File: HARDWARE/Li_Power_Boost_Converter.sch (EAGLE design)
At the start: 20 parts, among them U1 TPS61200

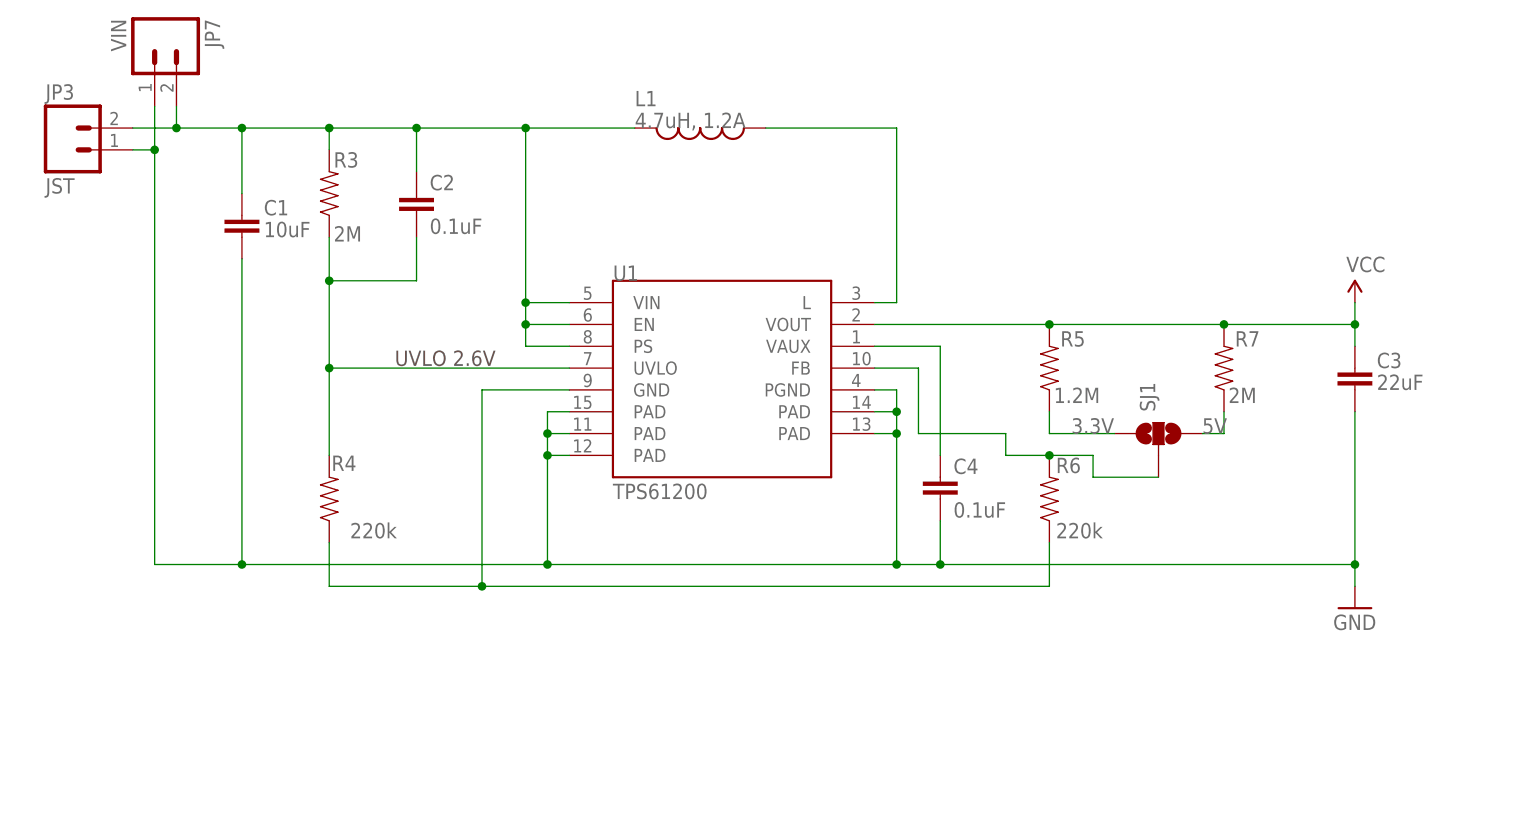
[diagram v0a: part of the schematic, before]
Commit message: Schematic Cleanup / Heat Sink
Cleaned up a few nets and removed on heat sink for better flow
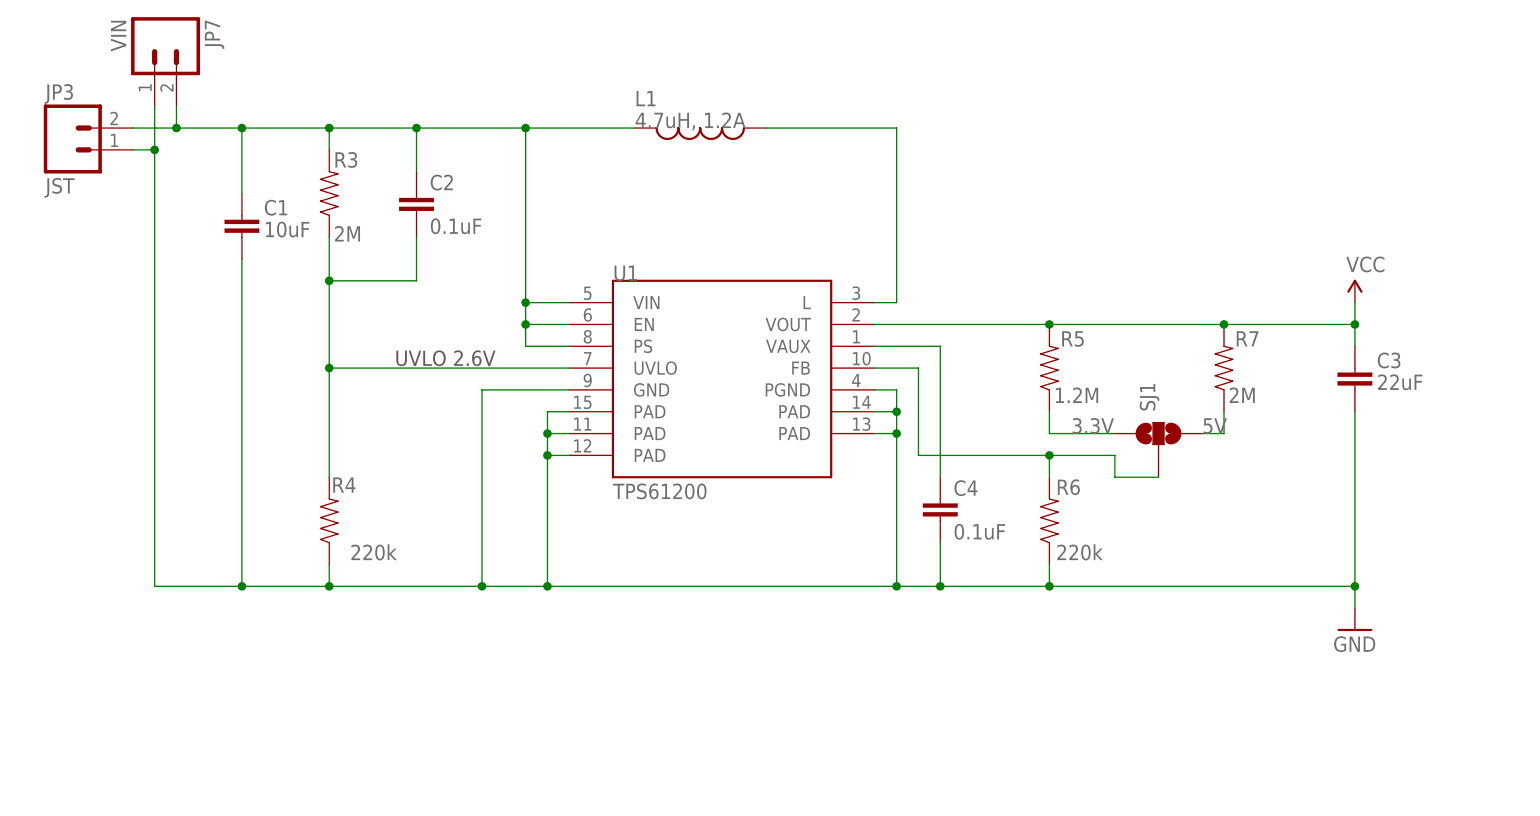
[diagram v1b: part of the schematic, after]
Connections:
- removed net GND1: R4.1, R6.1, U1.GND
- net GND: now also R4.1, R6.1, U1.GND
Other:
- moved on the sheet: C4, R4, R6
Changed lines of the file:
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@@
 <instance part="U1" gate="G$1" x="106.68" y="101.6"/>
 <instance part="C2" gate="G$1" x="71.12" y="119.38"/>
-<instance part="C4" gate="G$1" x="132.08" y="86.36"/>
+<instance part="C4" gate="G$1" x="132.08" y="83.82"/>
 <instance part="R3" gate="G$1" x="60.96" y="121.92" smashed="yes" rot="R90">
 <attribute name="NAME" x="61.468" y="124.9426" size="1.778" layer="95"/>
 <attribute name="VALUE" x="61.468" y="116.332" size="1.778" layer="96"/>
 </instance>
-<instance part="R4" gate="G$1" x="60.96" y="86.36" smashed="yes" rot="R90">
-<attribute name="NAME" x="61.214" y="89.6366" size="1.778" layer="95"/>
-<attribute name="VALUE" x="68.834" y="83.566" size="1.778" layer="96" rot="R180"/>
+<instance part="R4" gate="G$1" x="60.96" y="83.82" smashed="yes" rot="R90">
+<attribute name="NAME" x="61.214" y="87.0966" size="1.778" layer="95"/>
+<attribute name="VALUE" x="68.834" y="81.026" size="1.778" layer="96" rot="R180"/>
 </instance>
 <instance part="R5" gate="G$1" x="144.78" y="101.6" smashed="yes" rot="R90">
@@
 <attribute name="VALUE" x="145.288" y="97.536" size="1.778" layer="96"/>
 </instance>
-<instance part="R6" gate="G$1" x="144.78" y="86.36" smashed="yes" rot="R90">
-<attribute name="NAME" x="145.542" y="89.3826" size="1.778" layer="95"/>
-<attribute name="VALUE" x="145.542" y="81.788" size="1.778" layer="96"/>
-</instance>
-<instance part="GND1" gate="1" x="180.34" y="73.66"/>
+<instance part="R6" gate="G$1" x="144.78" y="83.82" smashed="yes" rot="R90">
+<attribute name="NAME" x="145.542" y="86.8426" size="1.778" layer="95"/>
+<attribute name="VALUE" x="145.542" y="79.248" size="1.778" layer="96"/>
+</instance>
+<instance part="GND1" gate="1" x="180.34" y="71.12"/>
 <instance part="GND2" gate="1" x="208.28" y="99.06"/>
 <instance part="R7" gate="G$1" x="165.1" y="101.6" smashed="yes" rot="R90">
@@
 <net name="N$1" class="0">
 <segment>
-<wire x1="132.08" y1="91.44" x2="132.08" y2="104.14" width="0.1524" layer="91"/>
+<wire x1="132.08" y1="88.9" x2="132.08" y2="104.14" width="0.1524" layer="91"/>
 <wire x1="132.08" y1="104.14" x2="124.46" y2="104.14" width="0.1524" layer="91"/>
 <pinref part="U1" gate="G$1" pin="VAUX"/>
@@
 <wire x1="60.96" y1="116.84" x2="60.96" y2="111.76" width="0.1524" layer="91"/>
 <wire x1="60.96" y1="111.76" x2="60.96" y2="101.6" width="0.1524" layer="91"/>
-<wire x1="60.96" y1="101.6" x2="60.96" y2="91.44" width="0.1524" layer="91"/>
+<wire x1="60.96" y1="101.6" x2="60.96" y2="88.9" width="0.1524" layer="91"/>
 <wire x1="88.9" y1="101.6" x2="60.96" y2="101.6" width="0.1524" layer="91"/>
 <wire x1="71.12" y1="116.84" x2="71.12" y2="111.76" width="0.1524" layer="91"/>
@@
 <net name="FB" class="0">
 <segment>
-<wire x1="129.54" y1="93.98" x2="139.7" y2="93.98" width="0.1524" layer="91"/>
-<wire x1="129.54" y1="93.98" x2="129.54" y2="101.6" width="0.1524" layer="91"/>
-<wire x1="129.54" y1="101.6" x2="124.46" y2="101.6" width="0.1524" layer="91"/>
-<wire x1="157.48" y1="88.9" x2="149.86" y2="88.9" width="0.1524" layer="91"/>
-<wire x1="149.86" y1="88.9" x2="149.86" y2="91.44" width="0.1524" layer="91"/>
-<wire x1="149.86" y1="91.44" x2="144.78" y2="91.44" width="0.1524" layer="91"/>
-<wire x1="144.78" y1="91.44" x2="139.7" y2="91.44" width="0.1524" layer="91"/>
-<wire x1="139.7" y1="91.44" x2="139.7" y2="93.98" width="0.1524" layer="91"/>
+<wire x1="144.78" y1="91.44" x2="152.4" y2="91.44" width="0.1524" layer="91"/>
+<wire x1="152.4" y1="91.44" x2="152.4" y2="88.9" width="0.1524" layer="91"/>
+<pinref part="SJ1" gate="G$1" pin="2"/>
+<wire x1="152.4" y1="88.9" x2="157.48" y2="88.9" width="0.1524" layer="91"/>
+<pinref part="R6" gate="G$1" pin="2"/>
+<wire x1="144.78" y1="88.9" x2="144.78" y2="91.44" width="0.1524" layer="91"/>
 <junction x="144.78" y="91.44"/>
+<wire x1="144.78" y1="91.44" x2="129.54" y2="91.44" width="0.1524" layer="91"/>
 <pinref part="U1" gate="G$1" pin="FB"/>
-<pinref part="R6" gate="G$1" pin="2"/>
-<pinref part="SJ1" gate="G$1" pin="2"/>
+<wire x1="124.46" y1="101.6" x2="129.54" y2="101.6" width="0.1524" layer="91"/>
+<wire x1="129.54" y1="101.6" x2="129.54" y2="91.44" width="0.1524" layer="91"/>
 </segment>
 </net>
@@
 <net name="GND" class="0">
 <segment>
-<wire x1="132.08" y1="83.82" x2="132.08" y2="78.74" width="0.1524" layer="91"/>
-<wire x1="50.8" y1="114.3" x2="50.8" y2="78.74" width="0.1524" layer="91"/>
-<wire x1="40.64" y1="127" x2="40.64" y2="78.74" width="0.1524" layer="91"/>
-<wire x1="40.64" y1="78.74" x2="50.8" y2="78.74" width="0.1524" layer="91"/>
-<wire x1="50.8" y1="78.74" x2="86.36" y2="78.74" width="0.1524" layer="91"/>
+<wire x1="213.36" y1="109.22" x2="208.28" y2="109.22" width="0.1524" layer="91"/>
+<wire x1="208.28" y1="109.22" x2="208.28" y2="101.6" width="0.1524" layer="91"/>
+<pinref part="GND2" gate="1" pin="GND"/>
+<pinref part="JP1" gate="G$1" pin="1"/>
+</segment>
+<segment>
+<wire x1="88.9" y1="99.06" x2="78.74" y2="99.06" width="0.1524" layer="91"/>
+<pinref part="U1" gate="G$1" pin="GND"/>
+<wire x1="132.08" y1="81.28" x2="132.08" y2="76.2" width="0.1524" layer="91"/>
+<wire x1="50.8" y1="114.3" x2="50.8" y2="76.2" width="0.1524" layer="91"/>
+<wire x1="40.64" y1="127" x2="40.64" y2="76.2" width="0.1524" layer="91"/>
+<wire x1="40.64" y1="76.2" x2="50.8" y2="76.2" width="0.1524" layer="91"/>
+<wire x1="50.8" y1="76.2" x2="60.96" y2="76.2" width="0.1524" layer="91"/>
+<wire x1="60.96" y1="76.2" x2="78.74" y2="76.2" width="0.1524" layer="91"/>
+<wire x1="78.74" y1="76.2" x2="86.36" y2="76.2" width="0.1524" layer="91"/>
 <wire x1="88.9" y1="96.52" x2="86.36" y2="96.52" width="0.1524" layer="91"/>
 <wire x1="86.36" y1="96.52" x2="86.36" y2="93.98" width="0.1524" layer="91"/>
@@
 <wire x1="86.36" y1="93.98" x2="86.36" y2="91.44" width="0.1524" layer="91"/>
 <wire x1="88.9" y1="91.44" x2="86.36" y2="91.44" width="0.1524" layer="91"/>
-<wire x1="86.36" y1="91.44" x2="86.36" y2="78.74" width="0.1524" layer="91"/>
-<wire x1="86.36" y1="78.74" x2="127" y2="78.74" width="0.1524" layer="91"/>
+<wire x1="86.36" y1="91.44" x2="86.36" y2="76.2" width="0.1524" layer="91"/>
+<wire x1="86.36" y1="76.2" x2="127" y2="76.2" width="0.1524" layer="91"/>
 <wire x1="124.46" y1="99.06" x2="127" y2="99.06" width="0.1524" layer="91"/>
 <wire x1="127" y1="99.06" x2="127" y2="96.52" width="0.1524" layer="91"/>
@@
 <wire x1="127" y1="96.52" x2="127" y2="93.98" width="0.1524" layer="91"/>
 <wire x1="124.46" y1="93.98" x2="127" y2="93.98" width="0.1524" layer="91"/>
-<wire x1="127" y1="93.98" x2="127" y2="78.74" width="0.1524" layer="91"/>
-<wire x1="127" y1="78.74" x2="132.08" y2="78.74" width="0.1524" layer="91"/>
-<wire x1="180.34" y1="78.74" x2="132.08" y2="78.74" width="0.1524" layer="91"/>
-<wire x1="180.34" y1="96.52" x2="180.34" y2="78.74" width="0.1524" layer="91"/>
+<wire x1="127" y1="93.98" x2="127" y2="76.2" width="0.1524" layer="91"/>
+<wire x1="127" y1="76.2" x2="132.08" y2="76.2" width="0.1524" layer="91"/>
+<wire x1="180.34" y1="76.2" x2="144.78" y2="76.2" width="0.1524" layer="91"/>
+<wire x1="144.78" y1="76.2" x2="132.08" y2="76.2" width="0.1524" layer="91"/>
+<wire x1="180.34" y1="96.52" x2="180.34" y2="76.2" width="0.1524" layer="91"/>
 <wire x1="40.64" y1="127" x2="38.1" y2="127" width="0.1524" layer="91"/>
-<wire x1="180.34" y1="78.74" x2="180.34" y2="76.2" width="0.1524" layer="91"/>
+<wire x1="180.34" y1="76.2" x2="180.34" y2="73.66" width="0.1524" layer="91"/>
 <wire x1="40.64" y1="132.08" x2="40.64" y2="127" width="0.1524" layer="91"/>
-<junction x="50.8" y="78.74"/>
+<junction x="50.8" y="76.2"/>
 <junction x="86.36" y="93.98"/>
 <junction x="86.36" y="91.44"/>
-<junction x="86.36" y="78.74"/>
+<junction x="86.36" y="76.2"/>
 <junction x="127" y="96.52"/>
 <junction x="127" y="93.98"/>
-<junction x="127" y="78.74"/>
-<junction x="132.08" y="78.74"/>
-<junction x="180.34" y="78.74"/>
+<junction x="127" y="76.2"/>
+<junction x="132.08" y="76.2"/>
+<junction x="180.34" y="76.2"/>
 <junction x="40.64" y="127"/>
 <pinref part="U1" gate="G$1" pin="PAD@1"/>
@@
 <pinref part="C1" gate="G$1" pin="2"/>
 <pinref part="JP7" gate="G$1" pin="1"/>
-</segment>
-<segment>
-<wire x1="213.36" y1="109.22" x2="208.28" y2="109.22" width="0.1524" layer="91"/>
-<wire x1="208.28" y1="109.22" x2="208.28" y2="101.6" width="0.1524" layer="91"/>
-<pinref part="GND2" gate="1" pin="GND"/>
-<pinref part="JP1" gate="G$1" pin="1"/>
+<pinref part="R4" gate="G$1" pin="1"/>
+<wire x1="60.96" y1="78.74" x2="60.96" y2="76.2" width="0.1524" layer="91"/>
+<junction x="60.96" y="76.2"/>
+<wire x1="78.74" y1="99.06" x2="78.74" y2="76.2" width="0.1524" layer="91"/>
+<junction x="78.74" y="76.2"/>
+<pinref part="R6" gate="G$1" pin="1"/>
+<wire x1="144.78" y1="78.74" x2="144.78" y2="76.2" width="0.1524" layer="91"/>
+<junction x="144.78" y="76.2"/>
 </segment>
 </net>
@@
 </segment>
 </net>
-<net name="GND1" class="0">
-<segment>
-<wire x1="88.9" y1="99.06" x2="78.74" y2="99.06" width="0.1524" layer="91"/>
-<wire x1="60.96" y1="76.2" x2="60.96" y2="81.28" width="0.1524" layer="91"/>
-<wire x1="144.78" y1="81.28" x2="144.78" y2="76.2" width="0.1524" layer="91"/>
-<wire x1="144.78" y1="76.2" x2="78.74" y2="76.2" width="0.1524" layer="91"/>
-<wire x1="78.74" y1="76.2" x2="60.96" y2="76.2" width="0.1524" layer="91"/>
-<wire x1="78.74" y1="99.06" x2="78.74" y2="76.2" width="0.1524" layer="91"/>
-<junction x="78.74" y="76.2"/>
-<pinref part="U1" gate="G$1" pin="GND"/>
-<pinref part="R4" gate="G$1" pin="1"/>
-<pinref part="R6" gate="G$1" pin="1"/>
-</segment>
-</net>

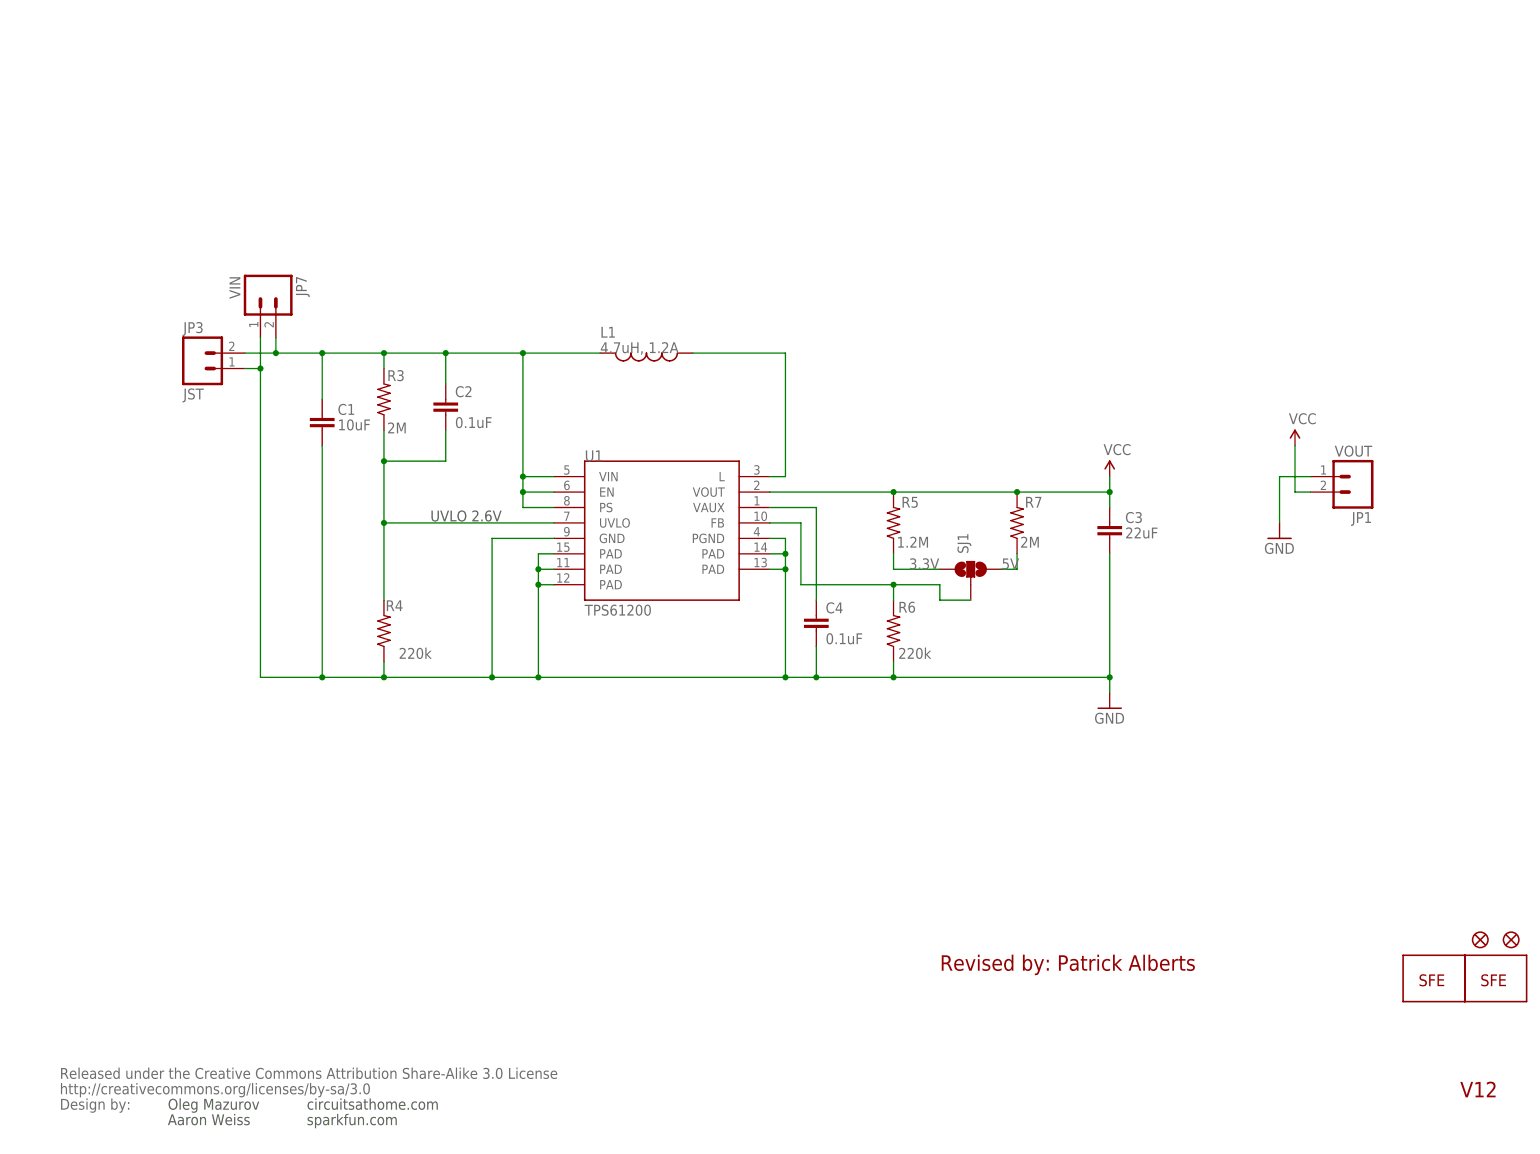
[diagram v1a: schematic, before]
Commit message: Trace Work
Routed all traces away from the Microcontroller, did a little trace
cleanup as well.
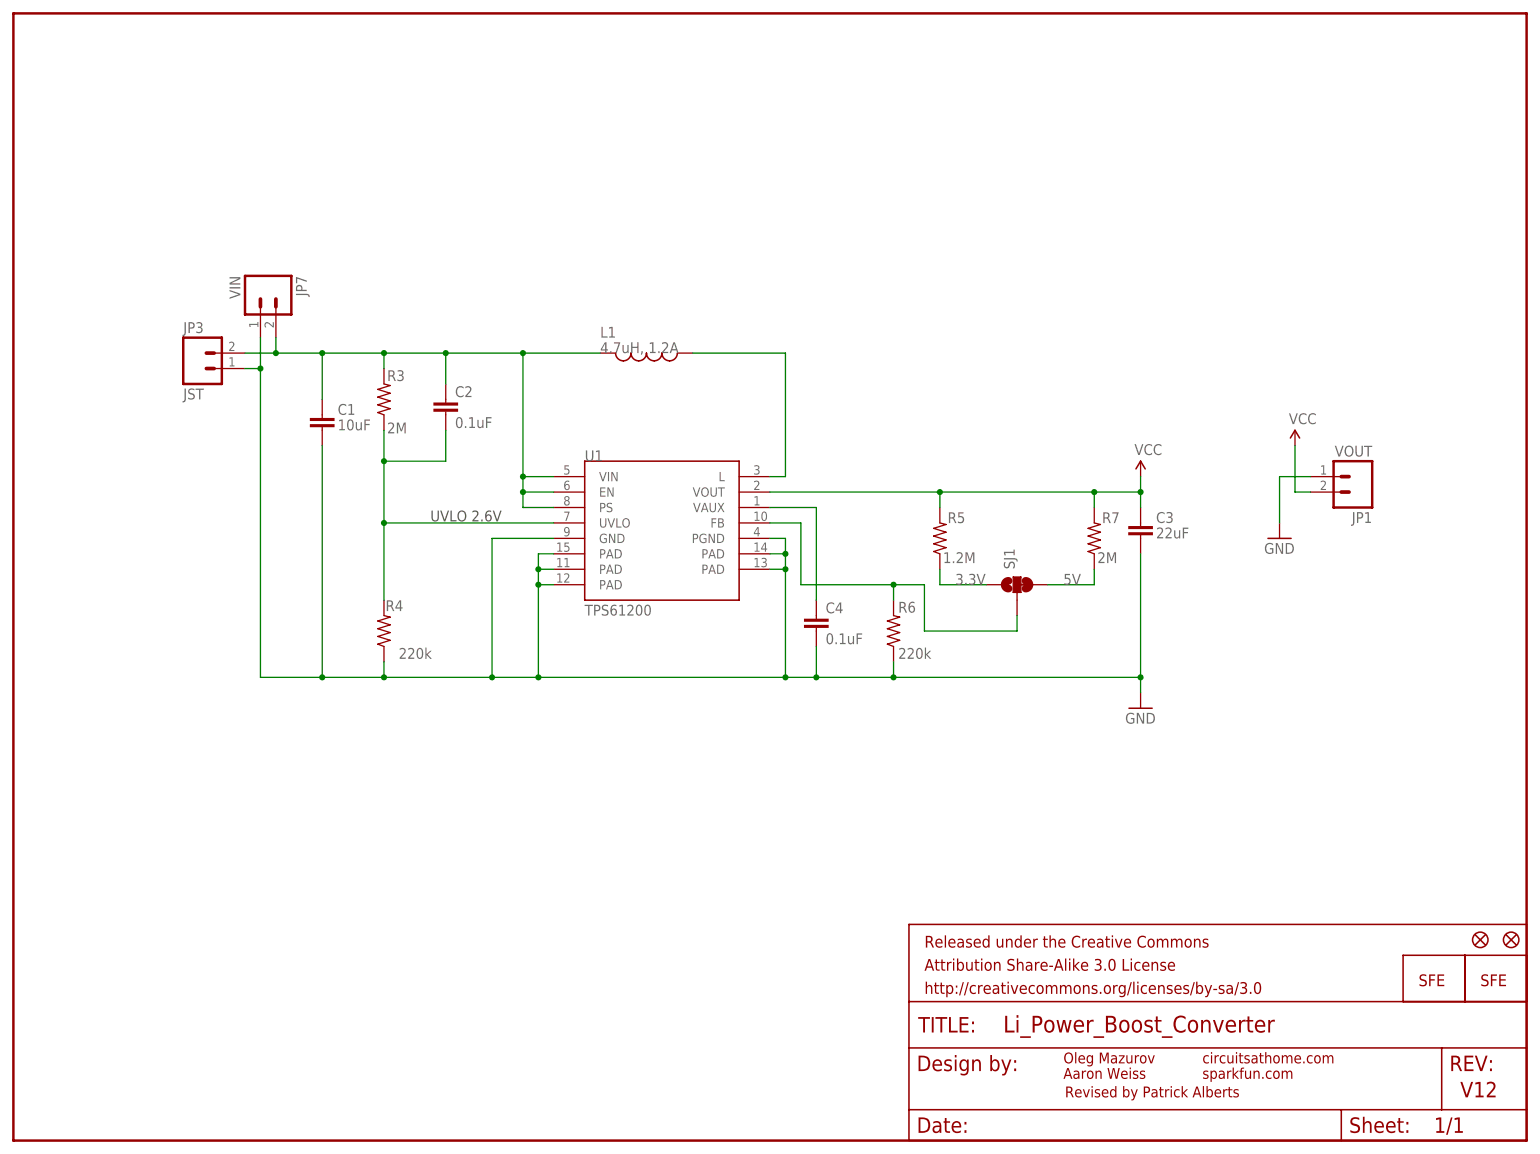
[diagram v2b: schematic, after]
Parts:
- removed U$1: CREATIVE_COMMONS, SparkFun:CREATIVE_COMMONS
- added FRAME1: FRAME-LETTER, SparkFun-Aesthetics:FRAME-LETTER
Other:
- note added: "Revised by Patrick Alberts"
- note removed: "Revised by: Patrick Alberts"
- moved on the sheet: C3, R5, R7, SJ1
